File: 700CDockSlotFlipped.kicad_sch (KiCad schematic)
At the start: 21 parts, among them J1 BUS_MCA, J10 GND, J100 Conn_02x60, J2 UPPER, J3 HPLA_PORT, J4 HPLA_PORT, J5 HPLA_PORT, J6 HPLA_PORT, J7 IRQ, J8 5V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

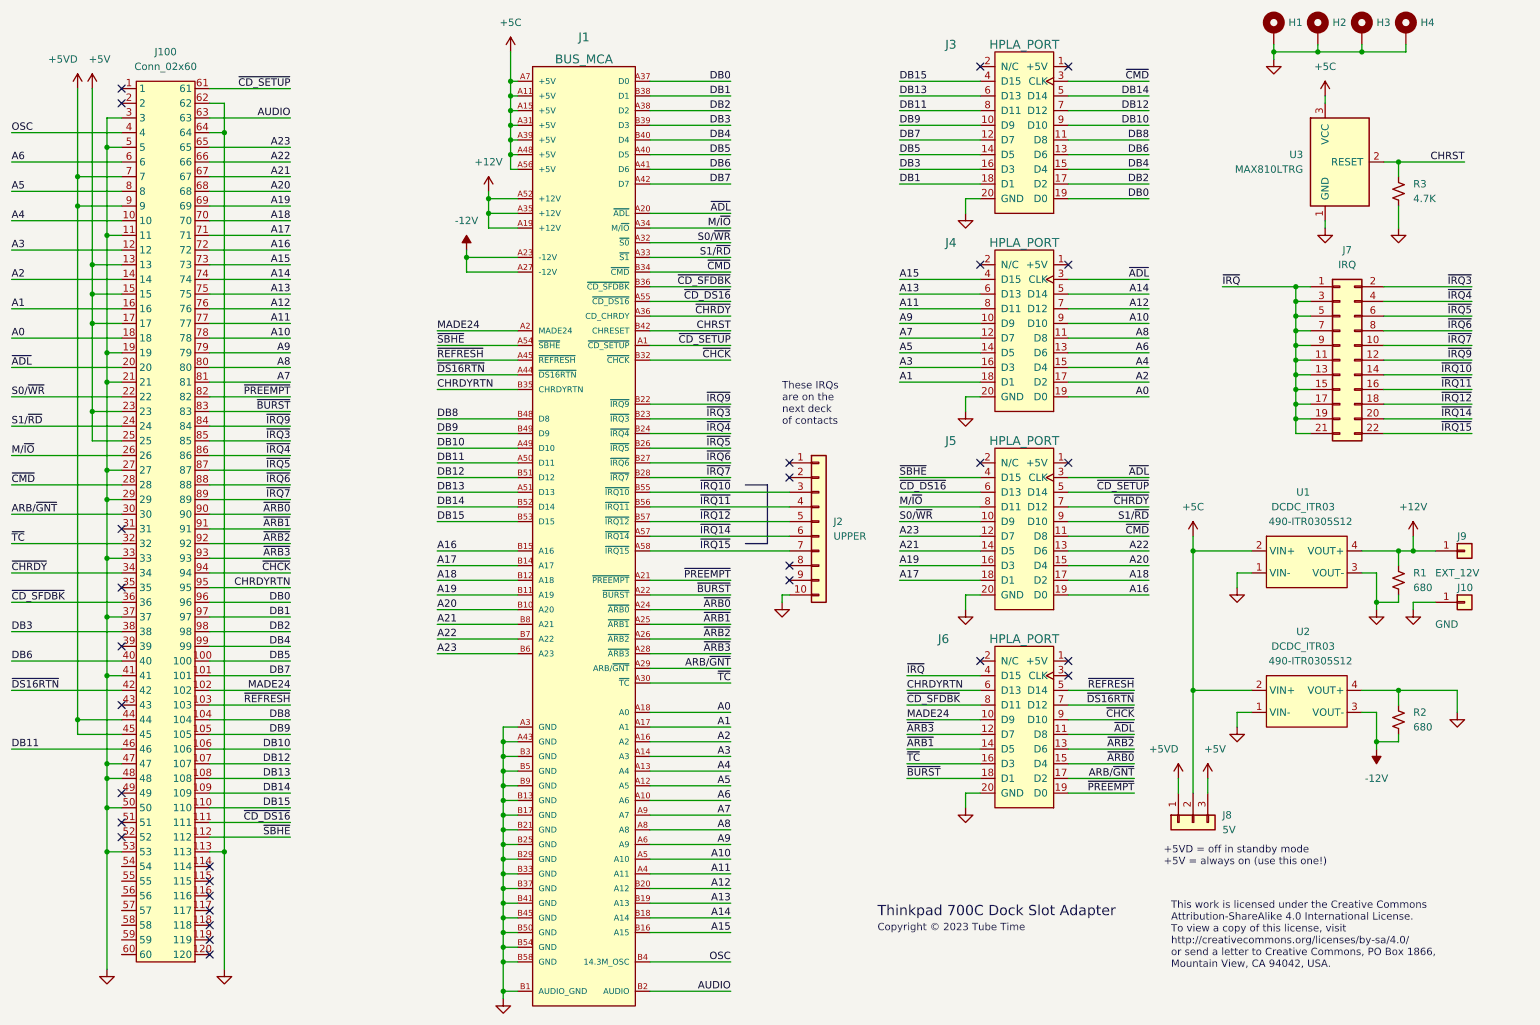
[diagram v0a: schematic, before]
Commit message: Rev 2: Fix CHRESET, disconnect and pull up MADE24
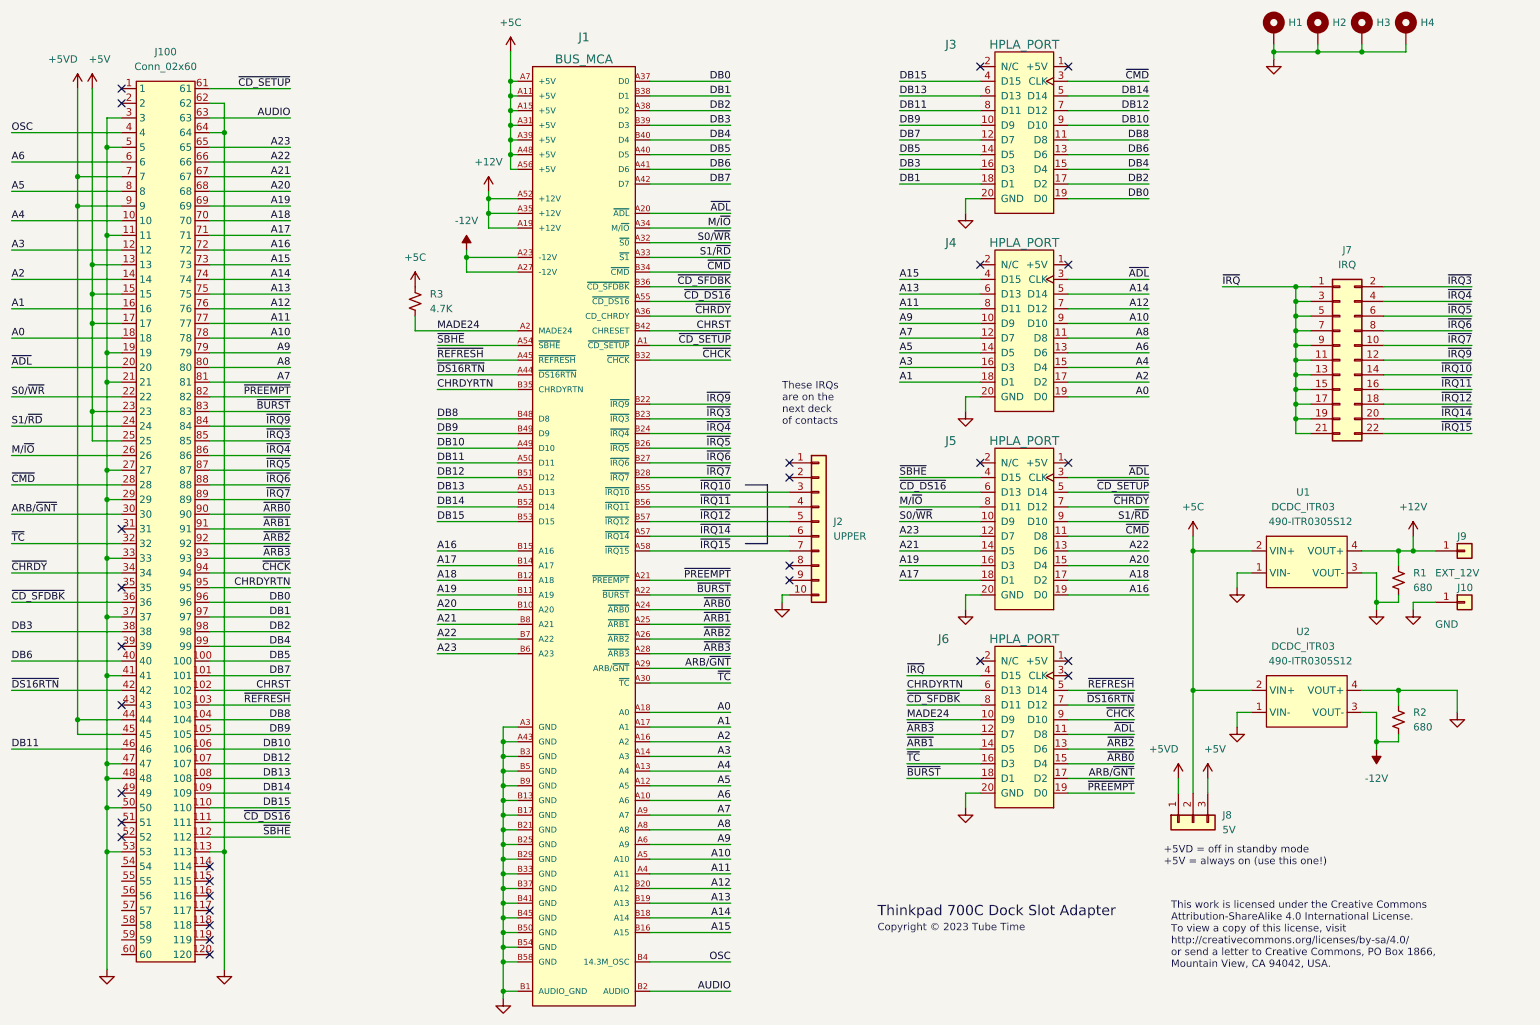
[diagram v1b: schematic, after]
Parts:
- removed U3: MAX810LTRG, Active:SOT95P230X117-3, symbol Power_Supervisor:TCM810
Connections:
- net +5C: now also R3.1
- net CHRST: now also J100.102; no longer R3.1
- net GND: no longer R3.2
- net MADE24: now also R3.2; no longer J100.102
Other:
- moved on the sheet: R3
